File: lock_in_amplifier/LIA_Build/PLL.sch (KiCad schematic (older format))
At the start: 0 parts

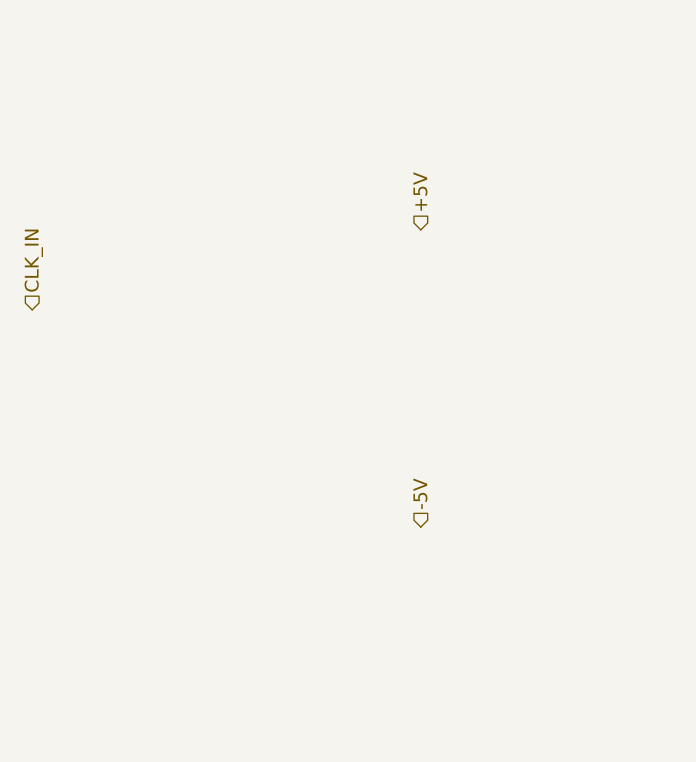
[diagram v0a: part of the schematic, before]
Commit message: switch footprints, lm833 usage, pll investigation
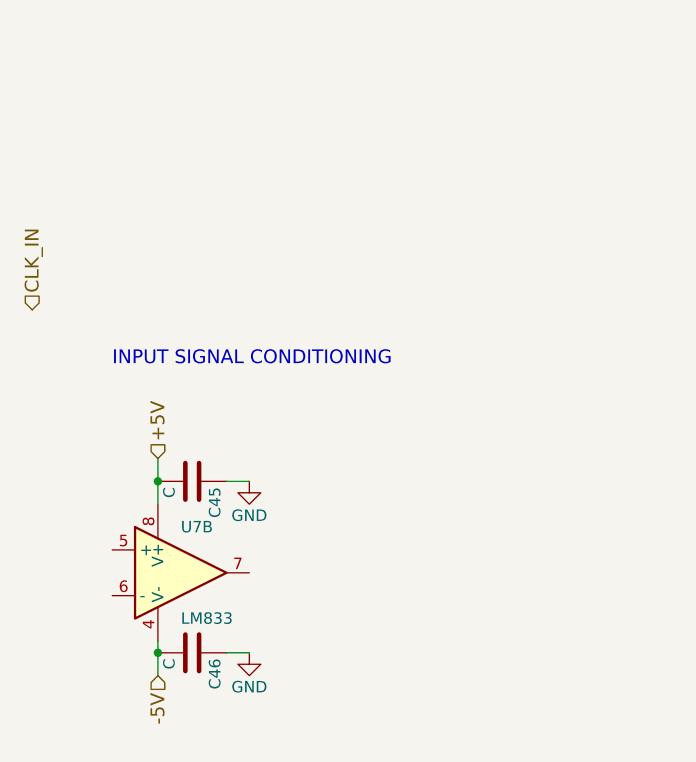
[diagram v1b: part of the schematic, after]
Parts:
- added C45, C46: C, symbol C
- added U7: LM833, symbol LM833
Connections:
- net +5V: now also C45.2, U7.8 (V+)
- net -5V: now also C46.2, U7.4 (V-)
- new net GND: C45.1, C46.1
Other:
- note added: "INPUT SIGNAL CONDITIONING"
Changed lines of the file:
@@
 Text HLabel 9000 2950 1    60   Input ~ 0
 CLK_OUT
-Text HLabel 3550 2500 1    60   Input ~ 0
+Text HLabel 2400 3500 1    60   Input ~ 0
 +5V
-Text HLabel 3550 3800 1    60   Input ~ 0
+Text HLabel 2400 4450 3    60   Input ~ 0
 -5V
 Text HLabel 5100 2650 1    60   Input ~ 0
@@
 Text Notes 1850 1550 0    60   ~ 0
 	•	PLL w/ divide for lock in?\n	◦	F, 2F modes\n	◦	PLL lock / unlock indicator LED\n	◦	Component selection, again...\n	◦	\n	◦	\n\n
+$Comp
+L LM833 U7
+U 2 1 5A262F93
+P 2500 4000
+F 0 "U7" H 2500 4200 50  0000 L CNN
+F 1 "LM833" H 2500 3800 50  0000 L CNN
+F 2 "" H 2500 4000 50  0001 C CNN
+F 3 "" H 2500 4000 50  0001 C CNN
+	2    2500 4000
+	1    0    0    -1
+$EndComp
+$Comp
+L C C46
+U 1 1 5A264DB1
+P 2550 4350
+F 0 "C46" H 2575 4450 50  0000 L CNN
+F 1 "C" H 2575 4250 50  0000 L CNN
+F 2 "" H 2588 4200 50  0001 C CNN
+F 3 "" H 2550 4350 50  0001 C CNN
+	1    2550 4350
+	0    1    1    0
+$EndComp
+$Comp
+L C C45
+U 1 1 5A264DDF
+P 2550 3600
+F 0 "C45" H 2575 3700 50  0000 L CNN
+F 1 "C" H 2575 3500 50  0000 L CNN
+F 2 "" H 2588 3450 50  0001 C CNN
+F 3 "" H 2550 3600 50  0001 C CNN
+	1    2550 3600
+	0    1    1    0
+$EndComp
+$Comp
+L GND #PWR076
+U 1 1 5A264E0E
+P 2800 3600
+F 0 "#PWR076" H 2800 3350 50  0001 C CNN
+F 1 "GND" H 2800 3450 50  0000 C CNN
+F 2 "" H 2800 3600 50  0001 C CNN
+F 3 "" H 2800 3600 50  0001 C CNN
+	1    2800 3600
+	1    0    0    -1
+$EndComp
+$Comp
+L GND #PWR077
+U 1 1 5A264E2B
+P 2800 4350
+F 0 "#PWR077" H 2800 4100 50  0001 C CNN
+F 1 "GND" H 2800 4200 50  0000 C CNN
+F 2 "" H 2800 4350 50  0001 C CNN
+F 3 "" H 2800 4350 50  0001 C CNN
+	1    2800 4350
+	1    0    0    -1
+$EndComp
+Wire Wire Line
+	2800 4350 2700 4350
+Wire Wire Line
+	2400 4300 2400 4450
+Connection ~ 2400 4350
+Wire Wire Line
+	2400 3500 2400 3700
+Connection ~ 2400 3600
+Wire Wire Line
+	2700 3600 2800 3600
+Text Notes 2200 3100 0    60   ~ 0
+INPUT SIGNAL CONDITIONING
 $EndSCHEMATC

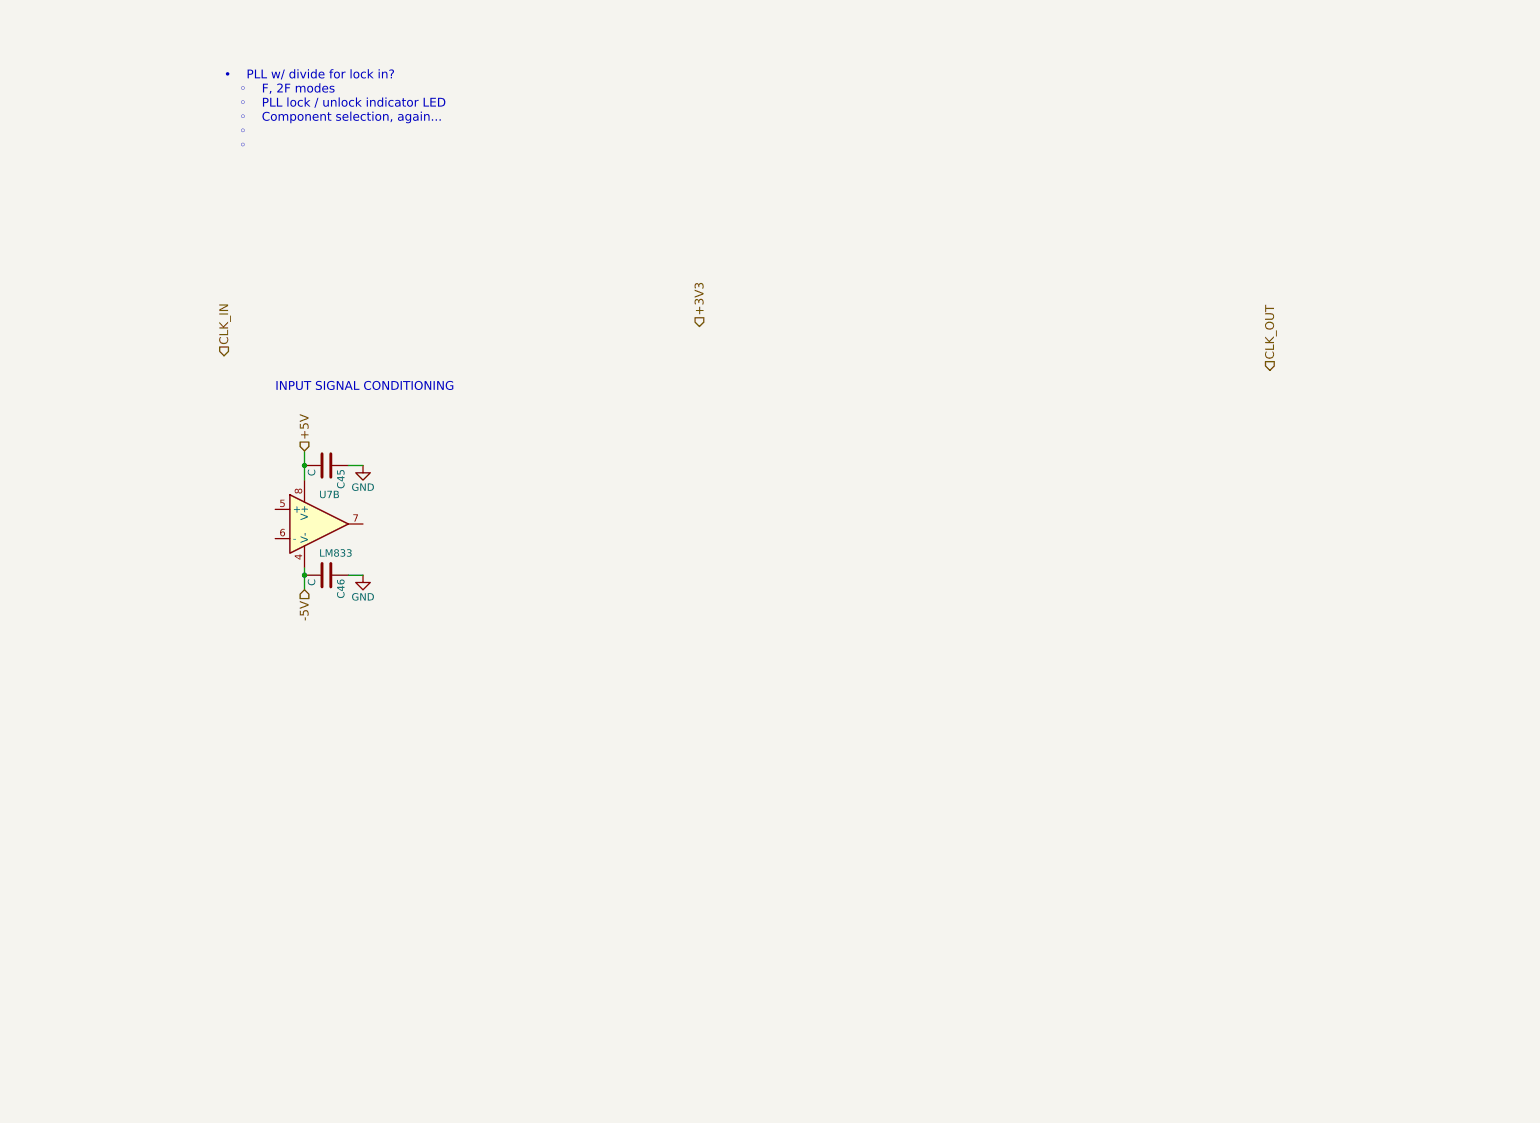
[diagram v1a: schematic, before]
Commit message: PLL initial implementation
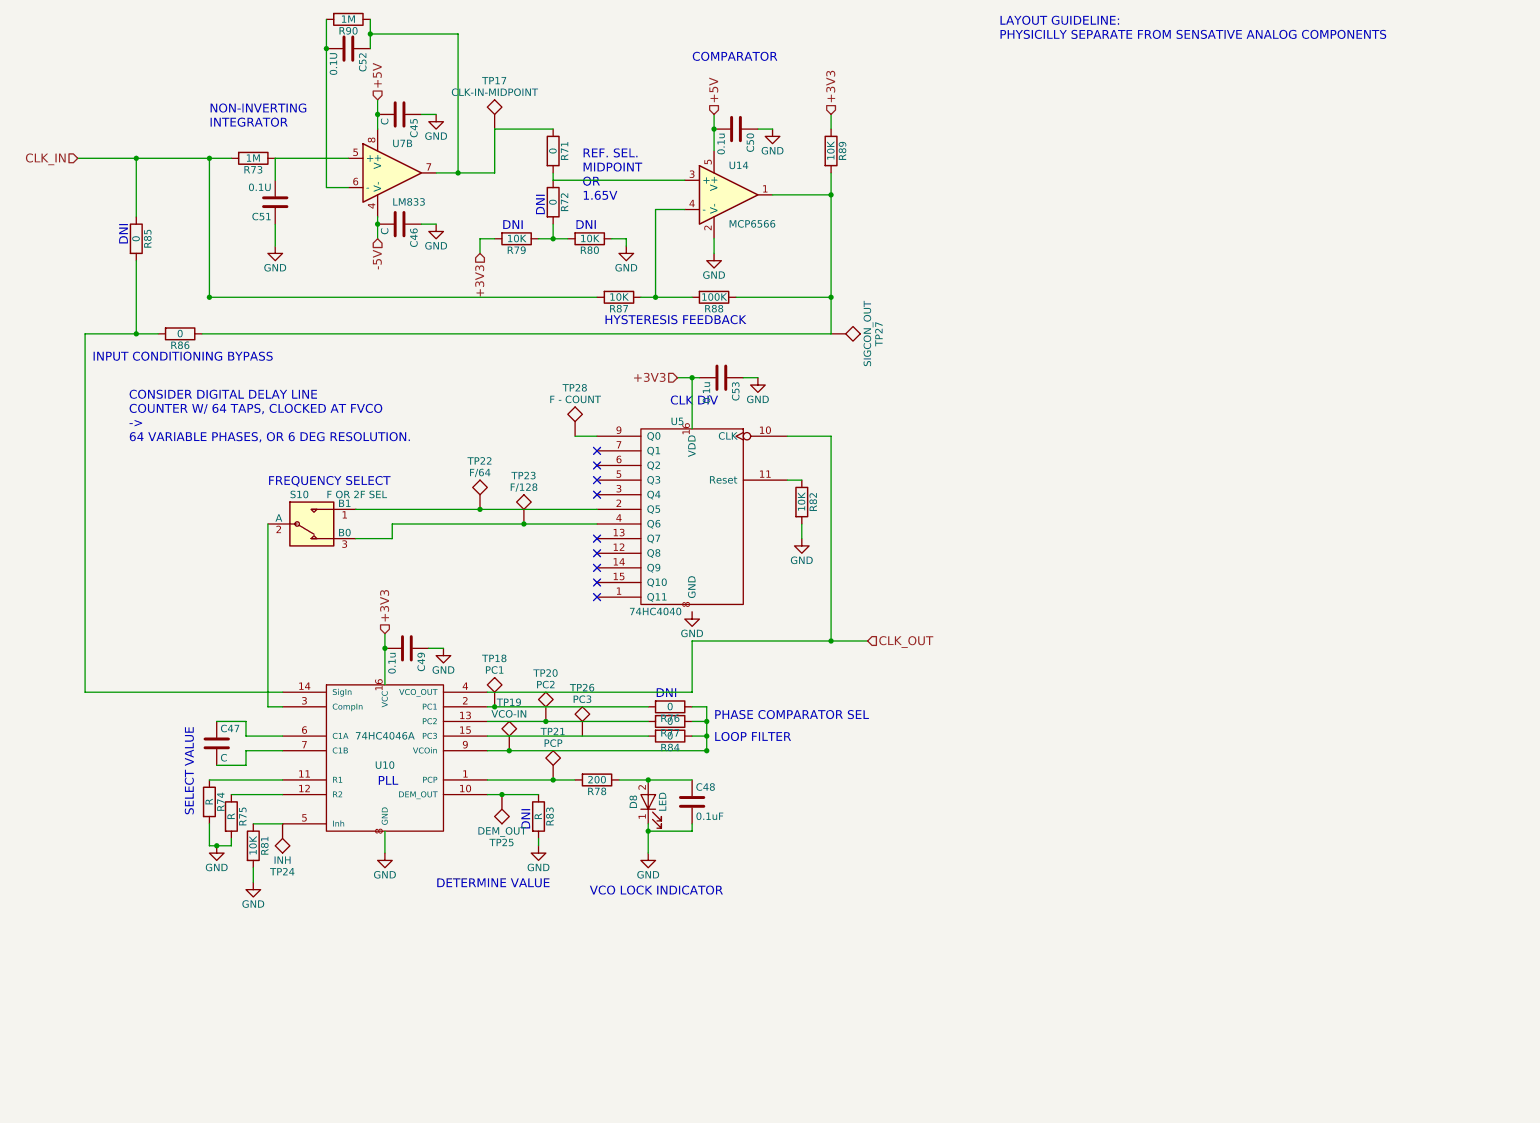
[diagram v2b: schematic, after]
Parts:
- added C47: C, symbol C
- added C48: 0.1uF, symbol C
- added C49, C50, C53: 0.1u, symbol C
- added C51, C52: 0.1U, symbol C
- added D8: LED, symbol LED
- added R71, R72, R76, R77, R84, R85, R86: 0, symbol R
- added R73, R90: 1M, symbol R
- added R74, R75, R83: R, symbol R
- added R78: 200, symbol R
- added R79, R80, R81, R82, R87, R89: 10K, symbol R
- added R88: 100K, symbol R
- added S10: F OR 2F SEL, symbol SPDT
- added TP17: CLK-IN-MIDPOINT, symbol TEST
- added TP18: PC1, symbol TEST
- added TP19: VCO-IN, symbol TEST
- added TP20: PC2, symbol TEST
- added TP21: PCP, symbol TEST
- added TP22: F/64, symbol TEST
- added TP23: F/128, symbol TEST
- added TP24: INH, symbol TEST
- added TP25: DEM_OUT, symbol TEST
- added TP26: PC3, symbol TEST
- added TP27: SIGCON_OUT, symbol TEST
- added TP28: F - COUNT, symbol TEST
- added U10: 74HC4046A, symbol 74HC4046A
- added U14: MCP6566, symbol MCP6566
- added U5: 74HC4040, symbol 74HC4040
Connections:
- net +3V3: now also C49.2, C53.2, R79.2, R89.1, U10.16 (VCC), U5.16 (VDD)
- net +5V: now also C50.2, U14.5 (V+)
- net CLK_IN: now also R73.2, R85.1, R87.2
- net CLK_OUT: now also U10.4 (VCO_OUT), U5.10 (CLK)
- net GND: now also C48.2, C49.1, C50.1, C51.1, C53.1, D8.1 (K), R74.2, R75.2, R80.1, R81.2, R82.2, R83.2, U10.8 (GND), U14.2 (V-)
- net at U7.5 (+): now also C51.2, R73.1
- net at U7.6 (-): now also C52.2, R90.2
- net at U7.7: now also C52.1, R71.1, R90.1, TP17.1
- new net: S10.1 (B1), TP22.1, U5.2 (Q5)
- new net: S10.2 (A), U10.3 (CompIn)
- new net: S10.3 (B0), TP23.1, U5.4 (Q6)
- new net: R71.2, R72.1, U14.3 (+)
- new net: R72.2, R79.1, R80.2
- new net: R76.1, R77.1, R84.1, TP19.1, U10.9 (VCOin)
- new net: R77.2, TP20.1, U10.13 (PC2)
- new net: R76.2, TP18.1, U10.2 (PC1)
- new net: C47.1, U10.6 (C1A)
- new net: C47.2, U10.7 (C1B)
- new net: R75.1, U10.12 (R2)
- new net: R74.1, U10.11 (R1)
- new net: R78.2, TP21.1, U10.1 (PCP)
- new net: C48.1, D8.2 (A), R78.1
- new net: R82.1, U5.11 (Reset)
- new net: R81.1, TP24.1, U10.5 (Inh)
- new net: R83.1, TP25.1, U10.10 (DEM_OUT)
- new net: R85.2, R86.2, U10.14 (SigIn)
- new net: R84.2, U10.15 (PC3)
- new net: R86.1, R88.1, R89.2, TP27.1, U14.1
- new net: TP28.1, U5.9 (Q0)
- new net: R87.1, R88.2, U14.4 (-)
- no-connect marks 0 -> 9
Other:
- note added: "CLK DIV"
- note added: "COMPARATOR"
- note added: "CONSIDER DIGITAL DELAY LINE\nCOUNTER W/ 64 TAPS, CLOCKED AT FVCO\n->\n64 VARIABLE PHASES, OR 6 DEG RESOLUTION.\n"
- note added: "DETERMINE VALUE"
- note added: "DNI"
- note added: "FREQUENCY SELECT"
- note added: "HYSTERESIS FEEDBACK"
- note added: "INPUT CONDITIONING BYPASS"
- note added: "LAYOUT GUIDELINE:\nPHYSICILLY SEPARATE FROM SENSATIVE ANALOG COMPONENTS"
- note added: "LOOP FILTER"
- note added: "NON-INVERTING\nINTEGRATOR"
- note added: "PHASE COMPARATOR SEL"
- note added: "PLL"
- note added: "REF. SEL.\nMIDPOINT\nOR\n1.65V"
- note added: "SELECT VALUE"
- note added: "VCO LOCK INDICATOR"
- note removed: "INPUT SIGNAL CONDITIONING"
- note removed: "• PLL w/ divide for lock in?\n ◦ F, 2F modes\n ◦ PLL lock / unlock indicator LED\n ◦ Component selection, again...\n ◦ \n ◦ \n\n"
- moved on the sheet: C45, C46, U7B

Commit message: Added quadrature demod, phase shift to pll
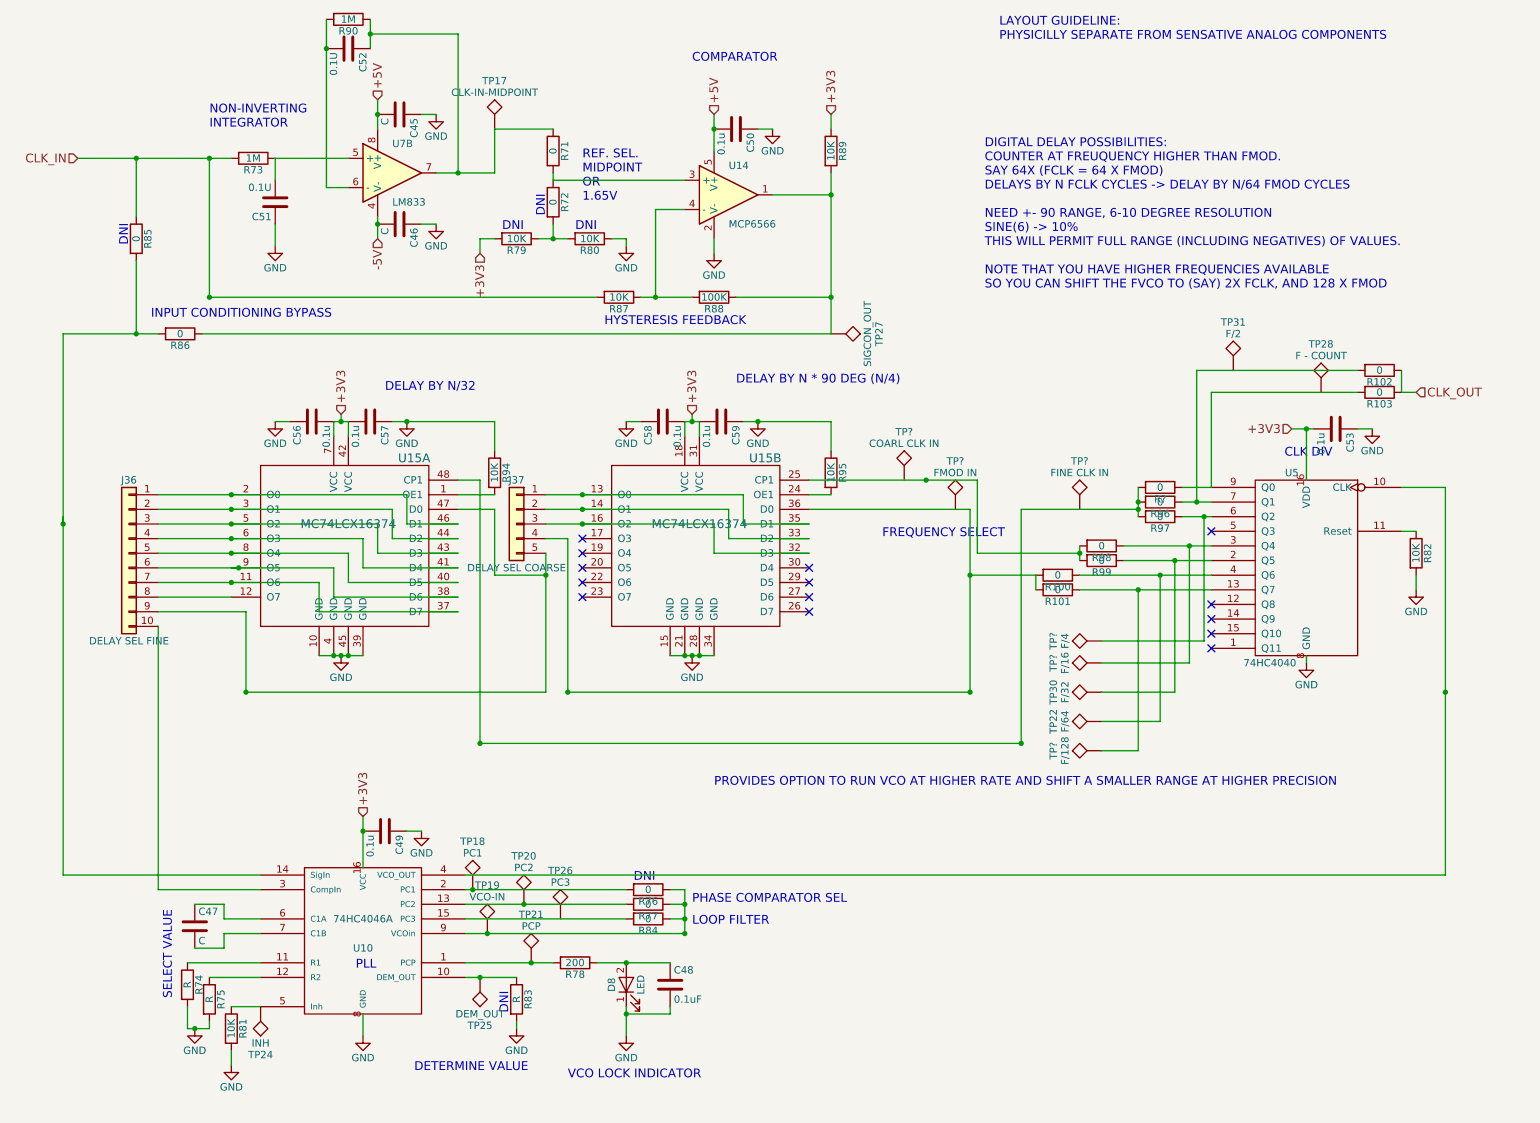
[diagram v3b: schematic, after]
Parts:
- removed S10: F OR 2F SEL, symbol SPDT
- removed TP23: F/128, symbol TEST
- added C56, C57, C58, C59: 0.1u, symbol C
- added J36: DELAY SEL FINE, symbol Conn_01x10
- added J37: DELAY SEL COARSE, symbol Conn_01x05
- added R100, R101, R102, R103, R96, R97, R98, R99, R?: 0, symbol R
- added R94, R95: 10K, symbol R
- added TP30: F/32, symbol TEST
- added TP31: F/2, symbol TEST
- added TP?: F/16, symbol TEST
- added TP?: F/128, symbol TEST
- added TP?: F/4, symbol TEST
- added TP?: COARL CLK IN, symbol TEST
- added TP?: FMOD IN, symbol TEST
- added TP?: FINE CLK IN, symbol TEST
- added U15: MC74LCX16374, symbol MC74LCX16374
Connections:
- net +3V3: now also C56.2, C57.2, C58.2, C59.2, U15.18 (VCC), U15.31 (VCC), U15.42 (VCC), U15.7 (VCC)
- net CLK_OUT: now also R102.1, R103.1; no longer U10.4 (VCO_OUT), U5.10 (CLK)
- net GND: now also U5.8 (GND), C56.1, C57.1, C58.1, C59.1, R94.1, R95.1, U15.10 (GND), U15.15 (GND), U15.21 (GND), U15.28 (GND), U15.34 (GND), U15.39 (GND), U15.4 (GND), U15.45 (GND)
- net at TP22.1: now also U5.4 (Q6), R100.1; no longer U5.2 (Q5)
- net at U10.3 (CompIn): now also J36.10 (Pin_10)
- net at TP28.1: no longer U5.9 (Q0)
- net at U5.13 (Q7): now also R101.1, TP?.1
- net at U5.3 (Q4): now also R98.1, TP?.1
- net at U5.6 (Q2): now also R97.1, TP?.1
- net at U5.7 (Q1): now also R102.2, R96.1
- new net: U10.4 (VCO_OUT), U5.10 (CLK)
- new net: J37.1 (Pin_1), U15.13 (O0), U15.35 (D1)
- new net: J37.2 (Pin_2), U15.14 (O1), U15.33 (D2)
- new net: J37.3 (Pin_3), U15.16 (O2), U15.32 (D3)
- new net: R95.2, U15.24 (OE1)
- new net: R98.2, R99.2, U15.25 (CP1)
- new net: J37.4 (Pin_4), R100.2, R101.2, U15.36 (D0)
- new net: R94.2, U15.1 (OE1)
- new net: J36.7 (Pin_7), U15.11 (O6), U15.37 (D7)
- new net: J36.8 (Pin_8), U15.12 (O7)
- new net: J36.1 (Pin_1), U15.2 (O0), U15.46 (D1)
- new net: J36.2 (Pin_2), U15.3 (O1), U15.44 (D2)
- new net: J36.6 (Pin_6), U15.38 (D6), U15.9 (O5)
- new net: J36.5 (Pin_5), U15.40 (D5), U15.8 (O4)
- new net: J36.4 (Pin_4), U15.41 (D4), U15.6 (O3)
- new net: J36.3 (Pin_3), U15.43 (D3), U15.5 (O2)
- new net: J36.9 (Pin_9), J37.5 (Pin_5), U15.47 (D0)
- new net: R96.2, R97.2, R?.2, U15.48 (CP1)
- new net: R99.1, TP30.1, U5.2 (Q5)
- new net: R103.2, R?.1, U5.9 (Q0)
- no-connect marks 9 -> 14
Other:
- note added: "DELAY BY N * 90 DEG (N/4)"
- note added: "DELAY BY N/32"
- note added: "DIGITAL DELAY POSSIBILITIES:\nCOUNTER AT FREUQUENCY HIGHER THAN FMOD.\nSAY 64X (FCLK = 64 X FMOD)\nDELAYS BY N FCLK CYCLES -> DELAY BY N/64 FMOD CYCLES\n\nNEED +- 90 RANGE, 6-10 DEGREE RESOLUTION\nSINE(6) -> 10%\nTHIS WILL PERMIT FULL RANGE (INCLUDING NEGATIVES) OF VALUES.\n\nNOTE THAT YOU HAVE HIGHER FREQUENCIES AVAILABLE \nSO YOU CAN SHIFT THE FVCO TO (SAY) 2X FCLK, AND 128 X FMOD"
- note added: "PROVIDES OPTION TO RUN VCO AT HIGHER RATE AND SHIFT A SMALLER RANGE AT HIGHER PRECISION"
- note removed: "CONSIDER DIGITAL DELAY LINE\nCOUNTER W/ 64 TAPS, CLOCKED AT FVCO\n->\n64 VARIABLE PHASES, OR 6 DEG RESOLUTION.\n"
- moved on the sheet: C47, C48, C49, C53, D8, R74, R75, R76, R77, R78, R81, R82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
